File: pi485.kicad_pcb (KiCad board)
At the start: 2 copper layers, 63 x 46 mm, 27 parts, among them J1 RS485, P1 Rasperry Pi, P2 PWR, P3 Term, P4 Latch Disable, Q1 2N4401, Q2 2N4401, Q3 2N4401, U1 NE555, U2 MAX485

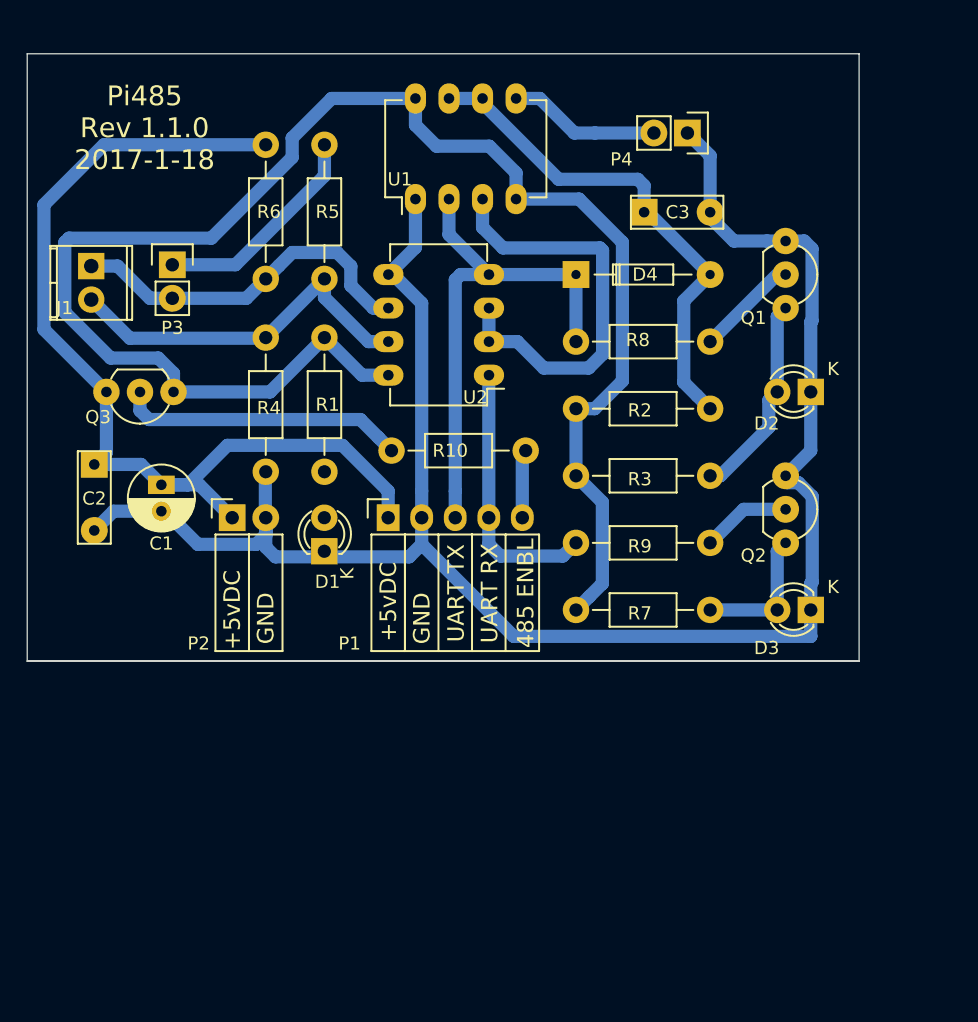
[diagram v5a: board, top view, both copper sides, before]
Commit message: * Added 3.3v enable / disable pin. Can be tied to 3.3v output on the pi, or a GPIO pin to force power off / on of the pi485 circuits. * Enables software control of a RS485 'reset', and will make it easier to support using LC-Tech 'carrier' boards in an alternate layout.
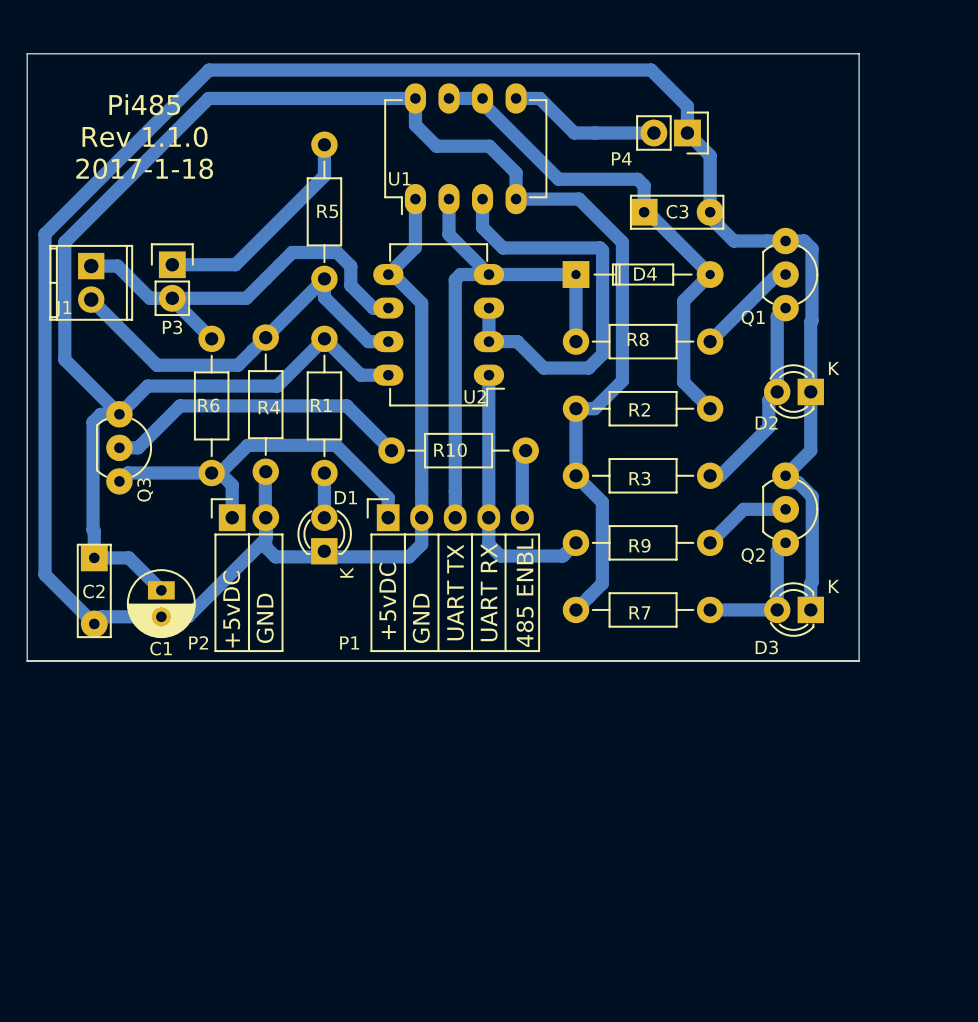
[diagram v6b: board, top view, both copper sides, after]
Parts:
- moved R1 10.3 mm to (34.9, 46.1), turned to 90 degrees
- moved C1 8.00 mm to (22.5, 55.0)
- moved C2 7.08 mm to (17.4, 52.5)
- moved R6 6.11 mm to (26.3, 35.9), turned to 270 degrees
- moved Q3 4.43 mm to (19.3, 41.6), turned to 270 degrees
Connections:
- C1 pad 1: VCC -> Net-(C1-Pad1)
- C2 pad 1: VCC -> Net-(C1-Pad1)
- Q3 pad 3: Net-(Q3-Pad3) -> Net-(C1-Pad1)
- R1 pad 1: Net-(Q3-Pad3) -> Net-(D1-Pad2)
- R1 pad 2: Net-(D1-Pad2) -> Net-(C1-Pad1)
- R2 pad 2: Net-(Q3-Pad3) -> Net-(C1-Pad1)
- R3 pad 2: VCC -> Net-(C1-Pad1)
- R7 pad 2: VCC -> Net-(C1-Pad1)
- U1 pad 4: Net-(Q3-Pad3) -> Net-(C1-Pad1)
- U1 pad 8: Net-(Q3-Pad3) -> Net-(C1-Pad1)
- U2 pad 8: Net-(Q3-Pad3) -> Net-(C1-Pad1)
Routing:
- net Net-(C1-Pad1): track 0.00 -> 142.7 mm
- net Net-(Q3-Pad3): track 110.5 -> 0.00 mm
- net VCC: track 86.5 -> 28.4 mm
- net GND: track 143.7 -> 199.7 mm
- net Net-(J1-Pad1): track 27.9 -> 32.2 mm
- net Net-(D1-Pad2): track 0.00 -> 3.39 mm
- net Net-(J1-Pad2): track 28.3 -> 30.1 mm
- net Net-(Q3-Pad2): track 21.7 -> 23.3 mm

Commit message: Hey look, mounting holes.
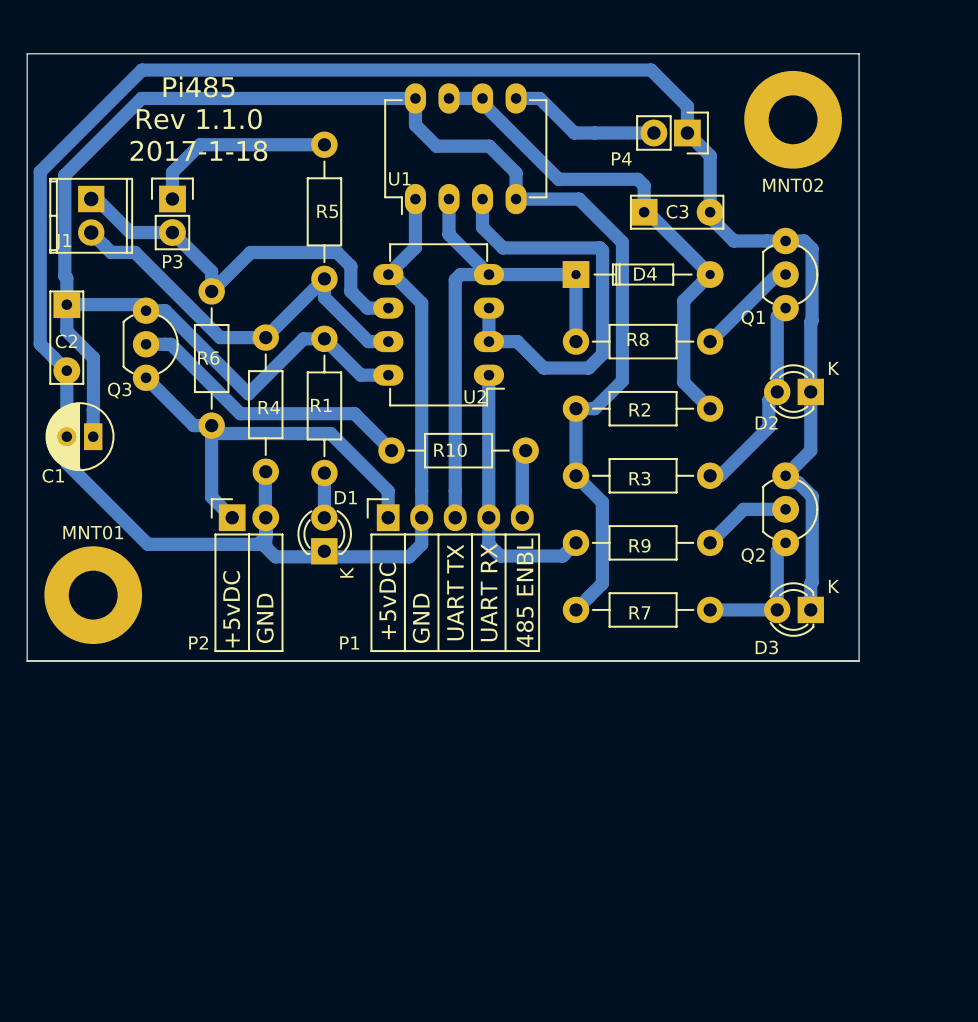
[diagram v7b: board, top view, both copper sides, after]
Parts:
- added MNT01: MountingHole_3.7mm_Pad, Mounting_Holes:MountingHole_3.7mm_Pad, F.Cu at (17.3, 55.3)
- added MNT02: MountingHole_3.7mm_Pad, Mounting_Holes:MountingHole_3.7mm_Pad, F.Cu at (70.3, 19.3)
- moved C2 19.3 mm to (15.3, 33.3)
- moved C1 12.7 mm to (17.3, 43.3), turned to 180 degrees
- moved Q3 8.10 mm to (21.3, 33.8)
- moved J1 5.08 mm to (17.2, 25.3)
- moved P3 4.98 mm to (23.3, 25.3)
- moved R6 3.59 mm to (26.3, 32.3)
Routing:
- net Net-(C1-Pad1): track 142.7 -> 134.0 mm
- net GND: track 199.7 -> 192.2 mm
- net VCC: track 28.4 -> 31.5 mm
- net Net-(P3-Pad1): track 16.7 -> 14.4 mm
- net Net-(J1-Pad1): track 32.2 -> 30.7 mm
- net Net-(Q3-Pad2): track 23.3 -> 21.9 mm
